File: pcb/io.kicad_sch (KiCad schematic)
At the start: 37 parts, among them J10 ARK2500R-A-2P, J2 RJ12, J3 RJ12, J4 Conn_02x05, J5 15EDGRC-3.5-03P, J6 15EDGRC-3.5-03P, J7 ARK2500R-A-2P, J8 ARK2500R-A-2P, J9 5EDGRC-3.5-02P, Q1 BT148, Q2 BC847, Q3 BC847, U7 6N137, U8 PC817, U9 PC817

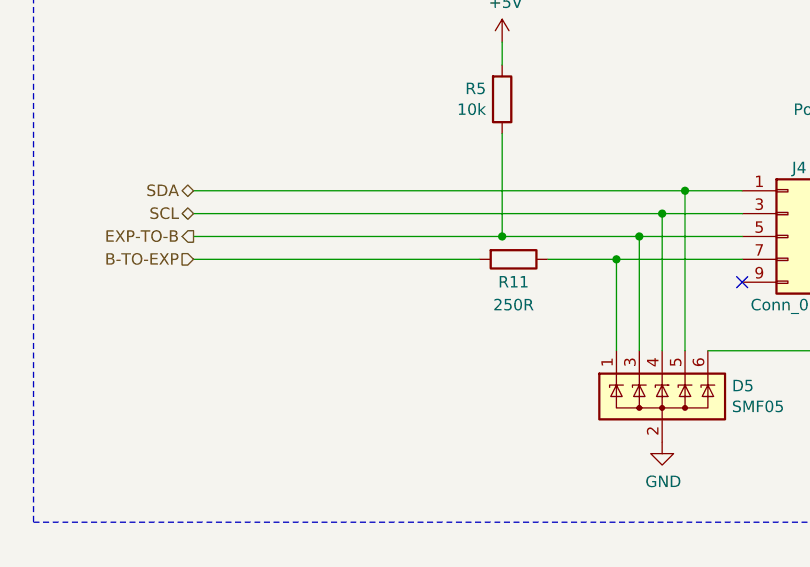
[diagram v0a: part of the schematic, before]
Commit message: Use polyfuse instead of resistor for main-exp protection.
Make voltage measurement possible.
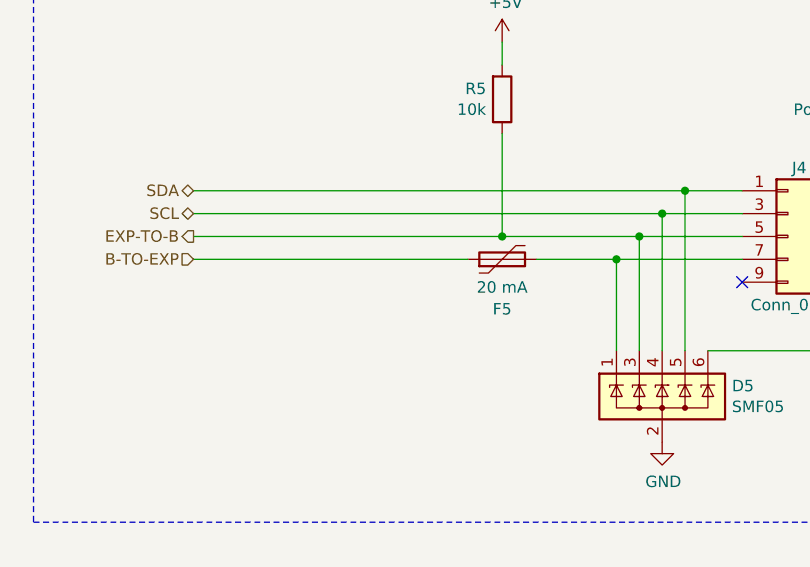
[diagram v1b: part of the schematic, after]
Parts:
- removed R11: 250R, Resistor_SMD:R_0805_2012Metric, symbol Device:R
- added F5: 20 mA, symbol Device:Polyfuse
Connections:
- net B-TO-EXP: now also F5.1
- net at D5.1 (K), J4.7 (Pin_7): now also F5.2
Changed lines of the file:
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@@
 	(wire
 		(pts
-			(xy 209.55 58.42) (xy 217.17 58.42)
+			(xy 208.28 58.42) (xy 217.17 58.42)
 		)
 		(stroke
@@
 	(wire
 		(pts
-			(xy 201.93 58.42) (xy 170.18 58.42)
+			(xy 200.66 58.42) (xy 170.18 58.42)
 		)
 		(stroke
@@
 	)
 	(symbol
-		(lib_id "Device:R")
-		(at 205.74 58.42 270)
-		(unit 1)
-		(exclude_from_sim no)
-		(in_bom yes)
-		(on_board yes)
-		(dnp no)
-		(property "Reference" "R11"
-			(at 205.74 60.96 90)
-			(effects
-				(font
-					(size 1.27 1.27)
-				)
-			)
-		)
-		(property "Value" "250R"
-			(at 205.74 63.5 90)
-			(effects
-				(font
-					(size 1.27 1.27)
-				)
-			)
-		)
-		(property "Footprint" "Resistor_SMD:R_0805_2012Metric"
-			(at 205.74 56.642 90)
-			(effects
-				(font
-					(size 1.27 1.27)
-				)
-				(hide yes)
-			)
-		)
-		(property "Datasheet" "~"
-			(at 205.74 58.42 0)
-			(effects
-				(font
-					(size 1.27 1.27)
-				)
-				(hide yes)
-			)
-		)
-		(property "Description" "Resistor"
-			(at 205.74 58.42 0)
-			(effects
-				(font
-					(size 1.27 1.27)
-				)
-				(hide yes)
-			)
-		)
-		(pin "1"
-		)
-		(pin "2"
-		)
-		(instances
-			(project ""
-				(path "/99e6b8eb-b08e-4d42-84dd-8b7f6765b7b7/00000000-0000-0000-0000-000061edd3fc"
-					(reference "R11")
-					(unit 1)
-				)
-			)
-		)
-	)
-	(symbol
 		(lib_id "power:+5V")
 		(at 251.46 34.29 0)
@@
 					(unit 1)
 				)
+			)
+		)
+	)
+	(symbol
+		(lib_id "Device:Polyfuse")
+		(at 204.47 58.42 90)
+		(unit 1)
+		(exclude_from_sim no)
+		(in_bom yes)
+		(on_board yes)
+		(dnp no)
+		(property "Reference" "F5"
+			(at 204.47 63.9615 90)
+			(effects
+				(font
+					(size 1.27 1.27)
+				)
+			)
+		)
+		(property "Value" "20 mA"
+			(at 204.47 61.5372 90)
+			(effects
+				(font
+					(size 1.27 1.27)
+				)
+			)
+		)
+		(property "Footprint" ""
+			(at 209.55 57.15 0)
+			(effects
+				(font
+					(size 1.27 1.27)
+				)
+				(justify left)
+				(hide yes)
+			)
+		)
+		(property "Datasheet" "~"
+			(at 204.47 58.42 0)
+			(effects
+				(font
+					(size 1.27 1.27)
+				)
+				(hide yes)
+			)
+		)
+		(property "Description" "Resettable fuse, polymeric positive temperature coefficient"
+			(at 204.47 58.42 0)
+			(effects
+				(font
+					(size 1.27 1.27)
+				)
+				(hide yes)
+			)
+		)
+		(pin "1"
+		)
+		(pin "2"
+		)
+		(instances
+			(project ""
+				(path "/99e6b8eb-b08e-4d42-84dd-8b7f6765b7b7/00000000-0000-0000-0000-000061edd3fc"
+					(reference "F5")
+					(unit 1)
+				)

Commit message: Add F5 missing footprint.
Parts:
- F5: footprint (none) -> Fuse:Fuse_1206_3216Metric
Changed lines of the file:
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@@
 			)
 		)
-		(property "Footprint" ""
+		(property "Footprint" "Fuse:Fuse_1206_3216Metric"
 			(at 209.55 57.15 0)
 			(effects

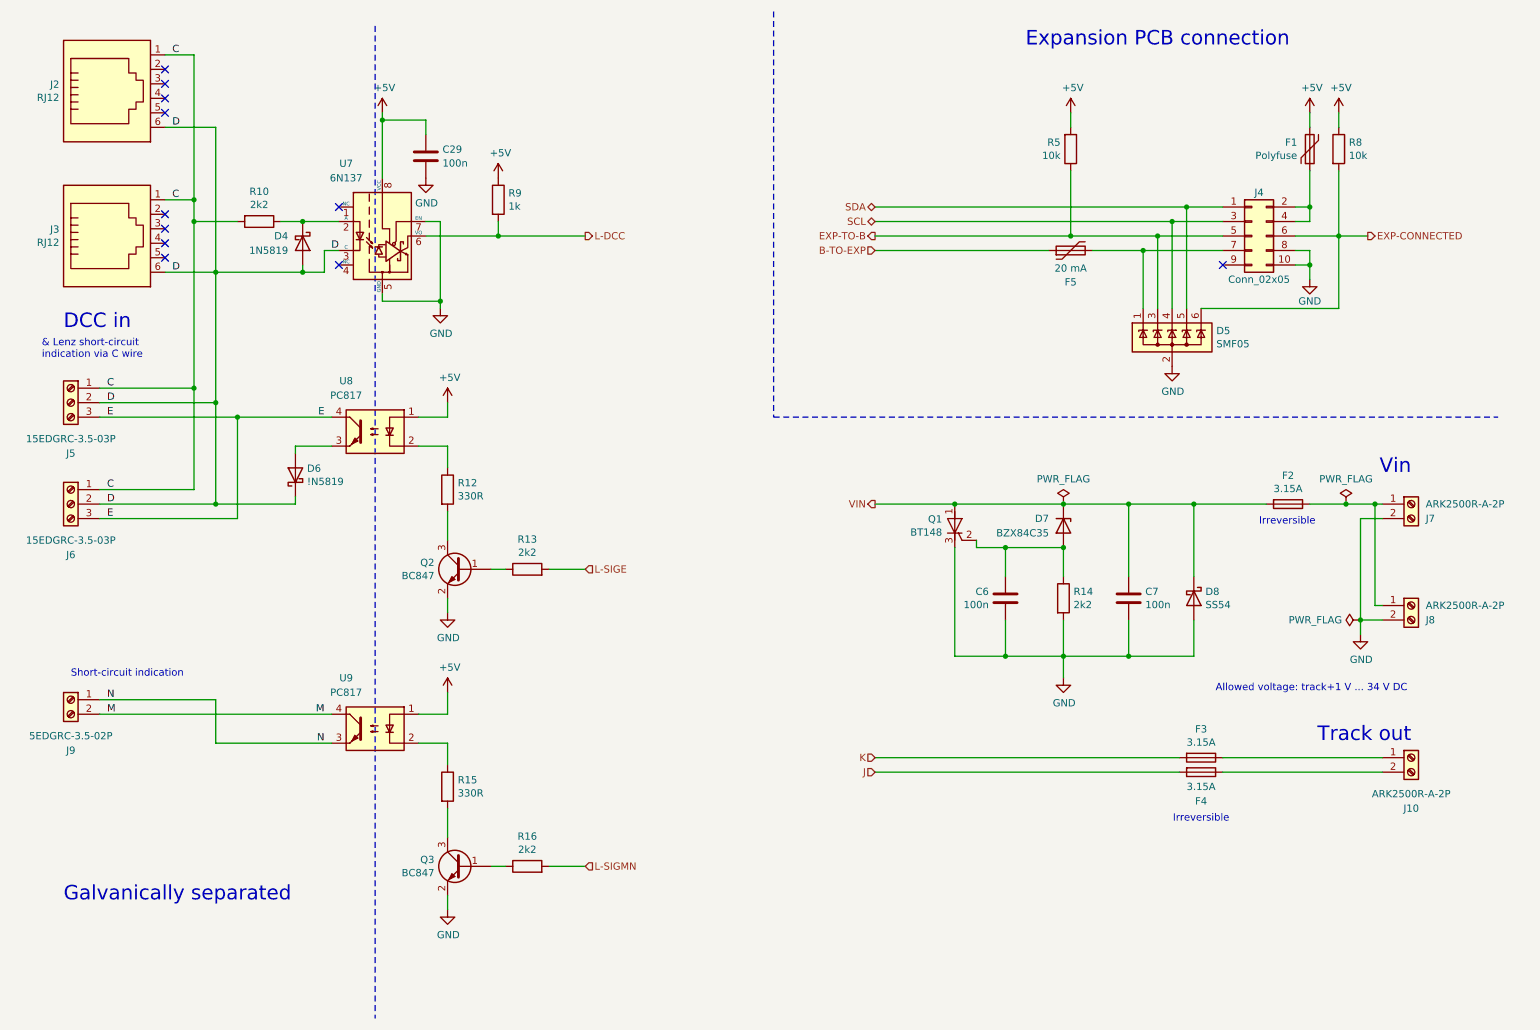
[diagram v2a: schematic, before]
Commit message: Use switched power supply for 5V internal.
78M05 would have 2.5 W of heat loss on it @ 30V input.
Other minor improvements.
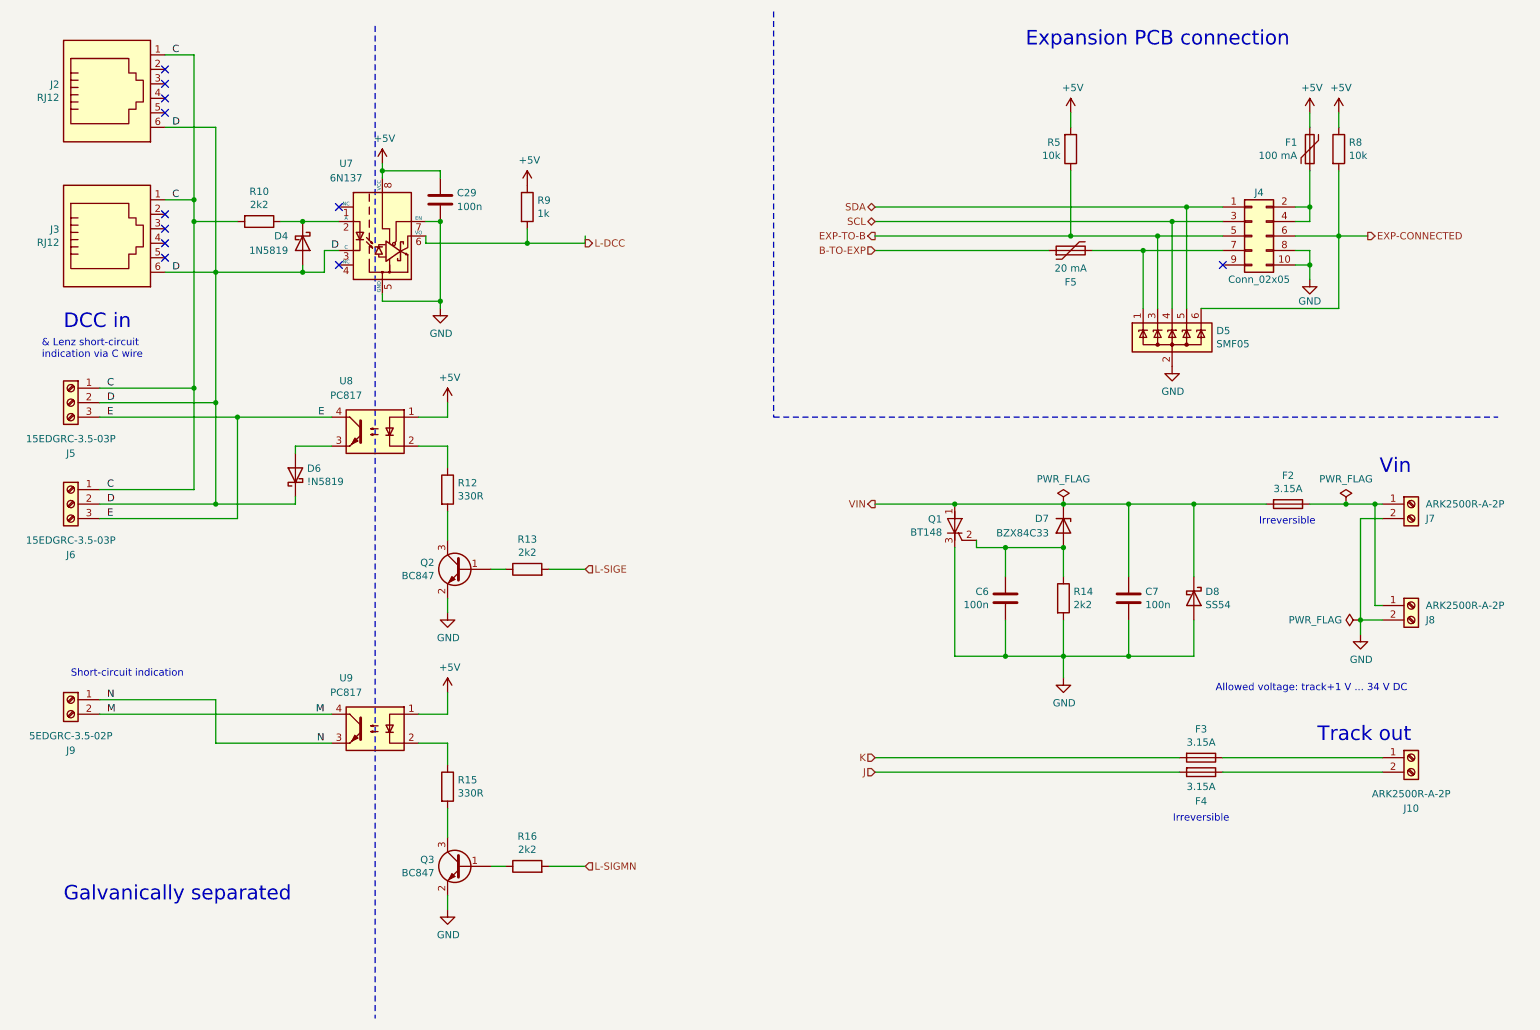
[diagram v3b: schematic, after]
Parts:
- D7: value BZX84C35 -> BZX84C33
- F1: value Polyfuse -> 100 mA; TME (none) -> PTS120660V010
- F5: TME (none) -> 0ZCM0002FF2G
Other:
- moved on the sheet: C29, R9
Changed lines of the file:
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@@
 	)
 	(junction
-		(at 83.82 35.56)
+		(at 93.98 53.34)
+		(diameter 0)
+		(color 0 0 0 0)
+	)
+	(junction
+		(at 83.82 44.45)
 		(diameter 0)
 		(color 0 0 0 0)
@@
 	)
 	(junction
-		(at 104.14 55.88)
+		(at 109.22 57.15)
 		(diameter 0)
 		(color 0 0 0 0)
@@
 	(wire
 		(pts
-			(xy 91.44 35.56) (xy 83.82 35.56)
+			(xy 93.98 44.45) (xy 83.82 44.45)
 		)
 		(stroke
@@
 	(wire
 		(pts
-			(xy 104.14 55.88) (xy 104.14 53.34)
+			(xy 109.22 57.15) (xy 109.22 54.61)
 		)
 		(stroke
@@
 	(wire
 		(pts
-			(xy 104.14 55.88) (xy 119.38 55.88)
+			(xy 109.22 57.15) (xy 119.38 57.15)
 		)
 		(stroke
@@
 	(wire
 		(pts
-			(xy 91.44 55.88) (xy 104.14 55.88)
+			(xy 91.44 57.15) (xy 109.22 57.15)
 		)
 		(stroke
@@
 	(wire
 		(pts
+			(xy 119.38 57.15) (xy 119.38 55.88)
+		)
+		(stroke
+			(width 0)
+			(type default)
+		)
+	)
+	(wire
+		(pts
 			(xy 219.71 68.58) (xy 219.71 55.88)
 		)
@@
 	(wire
 		(pts
-			(xy 83.82 35.56) (xy 83.82 34.29)
+			(xy 83.82 44.45) (xy 83.82 43.18)
 		)
 		(stroke
@@
 	(wire
 		(pts
+			(xy 91.44 57.15) (xy 91.44 55.88)
+		)
+		(stroke
+			(width 0)
+			(type default)
+		)
+	)
+	(wire
+		(pts
 			(xy 226.06 115.57) (xy 226.06 102.87)
 		)
@@
 	(wire
 		(pts
-			(xy 91.44 38.1) (xy 91.44 35.56)
+			(xy 93.98 45.72) (xy 93.98 44.45)
 		)
 		(stroke
@@
 	(wire
 		(pts
-			(xy 83.82 45.72) (xy 83.82 35.56)
+			(xy 83.82 45.72) (xy 83.82 44.45)
 		)
 		(stroke
@@
 	(hierarchical_label "L-DCC"
 		(shape output)
-		(at 119.38 55.88 0)
+		(at 119.38 57.15 0)
 		(effects
 			(font
@@
 			)
 		)
-		(property "Value" "Polyfuse"
+		(property "Value" "100 mA"
 			(at 244.1702 41.783 0)
 			(effects
@@
 			)
 		)
+		(property "TME" "PTS120660V010"
+			(at 246.38 40.64 0)
+			(effects
+				(font
+					(size 1.27 1.27)
+				)
+				(hide yes)
+			)
+		)
 		(pin "1"
 		)
@@
 	(symbol
 		(lib_id "power:+5V")
-		(at 83.82 34.29 0)
+		(at 83.82 43.18 0)
 		(unit 1)
 		(exclude_from_sim no)
@@
 		(dnp no)
 		(property "Reference" "#PWR0123"
-			(at 83.82 38.1 0)
+			(at 83.82 46.99 0)
 			(effects
 				(font
@@
 		)
 		(property "Value" "+5V"
-			(at 84.201 29.8958 0)
+			(at 84.201 38.7858 0)
 			(effects
 				(font
@@
 		)
 		(property "Footprint" ""
-			(at 83.82 34.29 0)
+			(at 83.82 43.18 0)
 			(effects
 				(font
@@
 		)
 		(property "Datasheet" ""
-			(at 83.82 34.29 0)
+			(at 83.82 43.18 0)
 			(effects
 				(font
@@
 		)
 		(property "Description" "Power symbol creates a global label with name \"+5V\""
-			(at 83.82 34.29 0)
+			(at 83.82 43.18 0)
 			(effects
 				(font
@@
 	(symbol
 		(lib_id "Device:R")
-		(at 104.14 49.53 0)
+		(at 109.22 50.8 0)
 		(unit 1)
 		(exclude_from_sim no)
@@
 		(dnp no)
 		(property "Reference" "R9"
-			(at 105.918 48.3616 0)
+			(at 110.998 49.6316 0)
 			(effects
 				(font
@@
 		)
 		(property "Value" "1k"
-			(at 105.918 50.673 0)
+			(at 110.998 51.943 0)
 			(effects
 				(font
@@
 		)
 		(property "Footprint" "Resistor_SMD:R_0805_2012Metric"
-			(at 102.362 49.53 90)
+			(at 107.442 50.8 90)
 			(effects
 				(font
@@
 		)
 		(property "Datasheet" "~"
-			(at 104.14 49.53 0)
+			(at 109.22 50.8 0)
 			(effects
 				(font
@@
 		)
 		(property "Description" "Resistor"
-			(at 104.14 49.53 0)
+			(at 109.22 50.8 0)
 			(effects
 				(font
@@
 	(symbol
 		(lib_id "power:+5V")
-		(at 104.14 45.72 0)
+		(at 109.22 46.99 0)
 		(unit 1)
 		(exclude_from_sim no)
@@
 		(dnp no)
 		(property "Reference" "#PWR0125"
-			(at 104.14 49.53 0)
+			(at 109.22 50.8 0)
 			(effects
 				(font
@@
 		)
 		(property "Value" "+5V"
-			(at 104.521 41.3258 0)
+			(at 109.601 42.5958 0)
 			(effects
 				(font
@@
 		)
 		(property "Footprint" ""
-			(at 104.14 45.72 0)
+			(at 109.22 46.99 0)
 			(effects
 				(font
@@
 		)
 		(property "Datasheet" ""
-			(at 104.14 45.72 0)
+			(at 109.22 46.99 0)
 			(effects
 				(font
@@
 		)
 		(property "Description" "Power symbol creates a global label with name \"+5V\""
-			(at 104.14 45.72 0)
+			(at 109.22 46.99 0)
 			(effects
 				(font
@@
 			)
 		)
-		(property "Value" "BZX84C35"
+		(property "Value" "BZX84C33"
 			(at 200.66 107.95 90)
 			(effects
@@
 			)
 		)
-		(pin "1"
-		)
-		(pin "2"
-		)
-		(instances
-			(project ""
-				(path "/99e6b8eb-b08e-4d42-84dd-8b7f6765b7b7/00000000-0000-0000-0000-000061edd3fc"
-					(reference "F5")
-					(unit 1)
-				)
-			)
-		)
-	)
-	(symbol
-		(lib_id "power:GND")
-		(at 91.44 45.72 0)
-		(unit 1)
-		(exclude_from_sim no)
-		(in_bom yes)
-		(on_board yes)
-		(dnp no)
-		(property "Reference" "#PWR011"
-			(at 91.44 52.07 0)
-			(effects
-				(font
-					(size 1.27 1.27)
-				)
-				(hide yes)
-			)
-		)
-		(property "Value" "GND"
-			(at 91.567 50.1142 0)
-			(effects
-				(font
-					(size 1.27 1.27)
-				)
-			)
-		)
-		(property "Footprint" ""
-			(at 91.44 45.72 0)
-			(effects
-				(font
-					(size 1.27 1.27)
-				)
-				(hide yes)
-			)
-		)
-		(property "Datasheet" ""
-			(at 91.44 45.72 0)
-			(effects
-				(font
-					(size 1.27 1.27)
-				)
-				(hide yes)
-			)
-		)
-		(property "Description" "Power symbol creates a global label with name \"GND\" , ground"
-			(at 91.44 45.72 0)
+		(property "TME" "0ZCM0002FF2G"
+			(at 204.47 58.42 90)
 			(effects
 				(font
@@
 		(pin "1"
 		)
+		(pin "2"
+		)
 		(instances
-			(project "hb22"
+			(project ""
 				(path "/99e6b8eb-b08e-4d42-84dd-8b7f6765b7b7/00000000-0000-0000-0000-000061edd3fc"
-					(reference "#PWR011")
+					(reference "F5")
 					(unit 1)
 				)
@@
 	(symbol
 		(lib_id "Device:C")
-		(at 91.44 41.91 0)
+		(at 93.98 49.53 0)
 		(unit 1)
 		(exclude_from_sim no)
@@
 		(fields_autoplaced yes)
 		(property "Reference" "C29"
-			(at 94.361 40.6978 0)
+			(at 96.901 48.3178 0)
 			(effects
 				(font
@@
 		)
 		(property "Value" "100n"
-			(at 94.361 43.1221 0)
+			(at 96.901 50.7421 0)
 			(effects
 				(font
@@
 		)
 		(property "Footprint" "Capacitor_SMD:C_0805_2012Metric"
-			(at 92.4052 45.72 0)
+			(at 94.9452 53.34 0)
 			(effects
 				(font
@@
 		)
 		(property "Datasheet" "~"
-			(at 91.44 41.91 0)
+			(at 93.98 49.53 0)
 			(effects
 				(font
@@
 		)
 		(property "Description" "Unpolarized capacitor"
-			(at 91.44 41.91 0)
+			(at 93.98 49.53 0)
 			(effects
 				(font

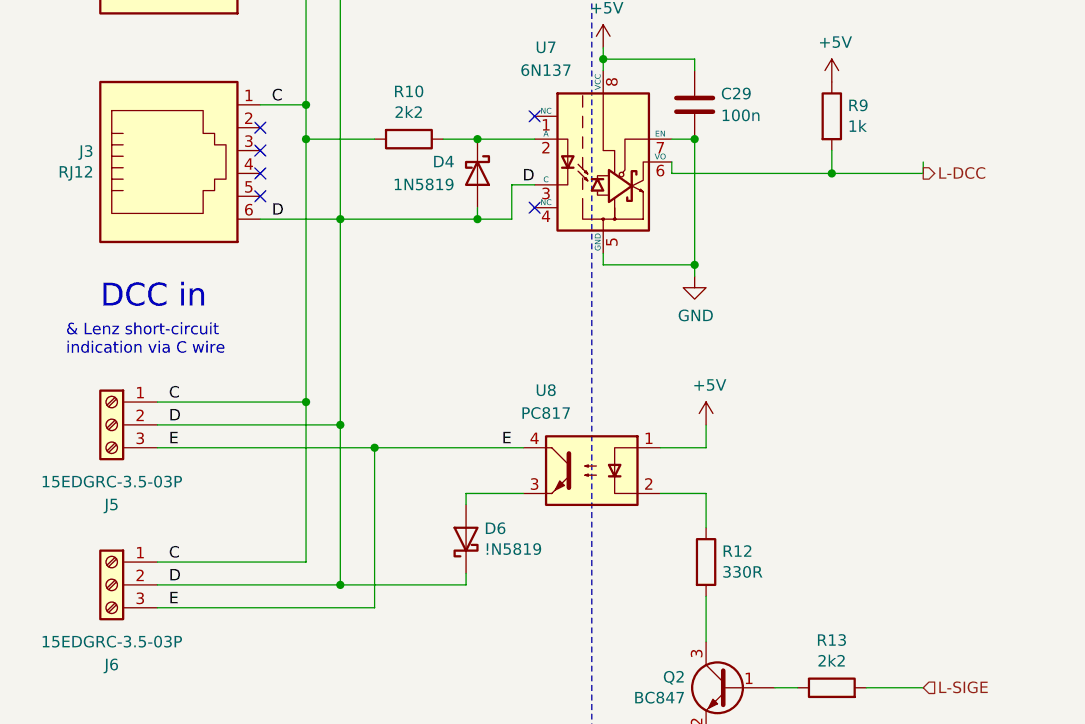
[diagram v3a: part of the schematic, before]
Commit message: Use ATmega328pb instead of ATmega328p.
Reason: obtain some free pins as a reserve.
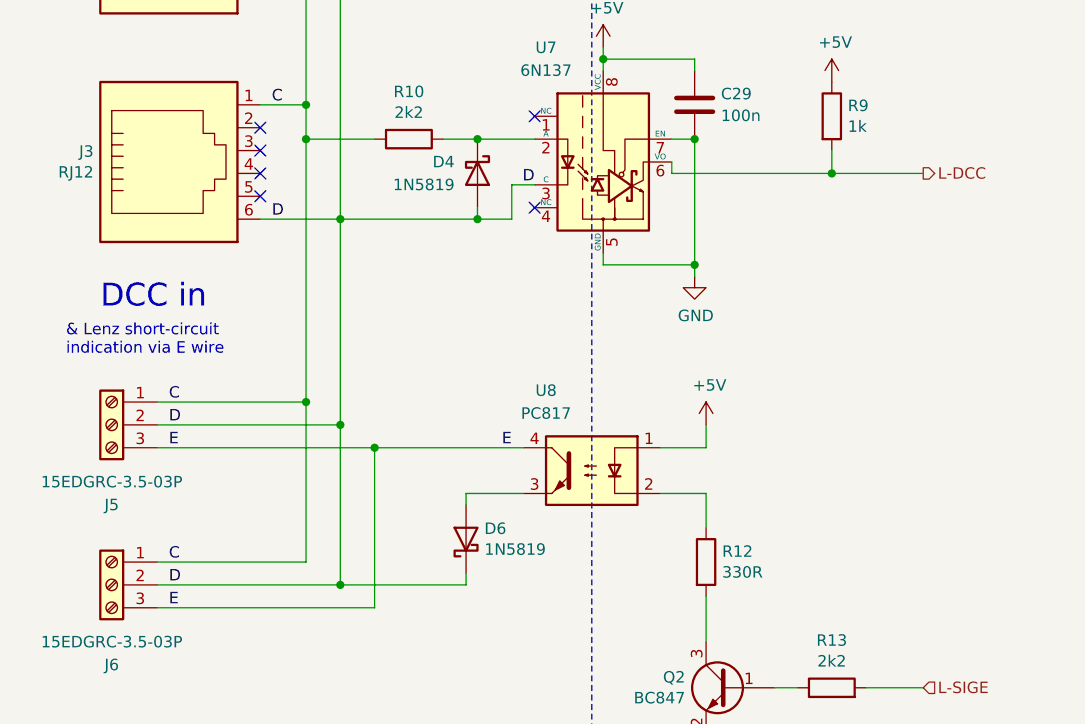
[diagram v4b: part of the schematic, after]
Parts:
- D6: value !N5819 -> 1N5819
- Q1: footprint Package_TO_SOT_THT:TO-92_Inline -> Package_TO_SOT_SMD:SOT-223
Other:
- note added: "& Lenz short-circuit indication via E wire"
- note removed: "& Lenz short-circuit indication via C wire"
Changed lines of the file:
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@@
 	(wire
 		(pts
-			(xy 119.38 57.15) (xy 119.38 55.88)
-		)
-		(stroke
-			(width 0)
-			(type default)
-		)
-	)
-	(wire
-		(pts
 			(xy 219.71 68.58) (xy 219.71 55.88)
 		)
@@
 		)
 	)
-	(text "& Lenz short-circuit\nindication via C wire"
+	(text "& Lenz short-circuit\nindication via E wire"
 		(exclude_from_sim no)
 		(at 24.13 77.47 0)
@@
 			)
 		)
-		(property "Value" "!N5819"
+		(property "Value" "1N5819"
 			(at 70.612 98.933 90)
 			(effects
@@
 			)
 		)
-		(property "Footprint" "Package_TO_SOT_THT:TO-92_Inline"
+		(property "Footprint" "Package_TO_SOT_SMD:SOT-223"
 			(at 181.61 108.585 0)
 			(effects
